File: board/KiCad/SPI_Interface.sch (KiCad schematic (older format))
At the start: 6 parts

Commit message: Finalize first draft
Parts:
- J2: renamed from J?; footprint Pinhead_1x6_TH -> Pin_Headers:Pin_Header_Straight_1x06
- R10, R11, R6, R9: renamed from R?; footprint (none) -> Resistors_SMD:R_0603_HandSoldering
- U4: renamed from U?; footprint (none) -> pmod:SOP2-8_Handsoldering
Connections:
- net 3V3_PMOD: now also U4.8 (VDD)
- net EXT_SPI_CLK: now also J2.2; no longer J2.4
- net EXT_SPI_MISO: now also J2.4; no longer J2.2
- no-connect marks 1 -> 0
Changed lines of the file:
@@
 $EndDescr
 $Comp
-L N25Q U?
+L N25Q U4
 U 1 1 56BBB08B
 P 5250 2850
-F 0 "U?" H 5050 2300 60  0000 C CNN
+F 0 "U4" H 5050 2300 60  0000 C CNN
 F 1 "N25Q" H 4950 3750 60  0000 C CNN
-F 2 "" H 5250 2850 60  0000 C CNN
+F 2 "pmod:SOP2-8_Handsoldering" H 5250 2850 60  0001 C CNN
 F 3 "" H 5250 2850 60  0000 C CNN
 	1    5250 2850
@@
 Wire Wire Line
 	1600 1300 7550 1300
-Wire Wire Line
-	5250 1300 5250 1900
-$Comp
-L GND #PWR?
+$Comp
+L GND #PWR22
 U 1 1 56BCE787
 P 5250 3800
-F 0 "#PWR?" H 5250 3550 50  0001 C CNN
+F 0 "#PWR22" H 5250 3550 50  0001 C CNN
 F 1 "GND" H 5250 3650 50  0000 C CNN
 F 2 "" H 5250 3800 60  0000 C CNN
@@
 	5250 3800 5250 3500
 $Comp
-L R R?
+L R R9
 U 1 1 56BCEBB1
 P 7050 2500
-F 0 "R?" V 7130 2500 50  0000 C CNN
+F 0 "R9" V 7130 2500 50  0000 C CNN
 F 1 "10k" V 7050 2500 50  0000 C CNN
-F 2 "" V 6980 2500 30  0000 C CNN
+F 2 "Resistors_SMD:R_0603_HandSoldering" V 6980 2500 30  0001 C CNN
 F 3 "" H 7050 2500 30  0000 C CNN
 	1    7050 2500
@@
 $EndComp
 $Comp
-L R R?
+L R R10
 U 1 1 56BCEC4A
 P 7300 2500
-F 0 "R?" V 7380 2500 50  0000 C CNN
+F 0 "R10" V 7380 2500 50  0000 C CNN
 F 1 "10k" V 7300 2500 50  0000 C CNN
-F 2 "" V 7230 2500 30  0000 C CNN
+F 2 "Resistors_SMD:R_0603_HandSoldering" V 7230 2500 30  0001 C CNN
 F 3 "" H 7300 2500 30  0000 C CNN
 	1    7300 2500
@@
 $EndComp
 $Comp
-L R R?
+L R R11
 U 1 1 56BCEC79
 P 7550 2500
-F 0 "R?" V 7630 2500 50  0000 C CNN
+F 0 "R11" V 7630 2500 50  0000 C CNN
 F 1 "10k" V 7550 2500 50  0000 C CNN
-F 2 "" V 7480 2500 30  0000 C CNN
+F 2 "Resistors_SMD:R_0603_HandSoldering" V 7480 2500 30  0001 C CNN
 F 3 "" H 7550 2500 30  0000 C CNN
 	1    7550 2500
@@
 EXT_SPI_SS_B
 Connection ~ 4400 2950
-NoConn ~ 8200 1800
 Text GLabel 1550 2150 0    60   Input ~ 0
 ICE_SDO
@@
 ICE_SDI
 Wire Wire Line
-	5900 2350 5950 2350
-Wire Wire Line
-	5950 2350 5950 1950
-Wire Wire Line
-	5950 1950 1550 1950
+	5950 2350 5900 2350
+Wire Wire Line
+	5950 1800 5950 2350
 Text GLabel 1700 2800 0    60   Input ~ 0
 EXT_SPI_MISO
@@
 Connection ~ 3650 2350
 $Comp
-L R R?
+L R R6
 U 1 1 56BD0F26
 P 4350 1600
-F 0 "R?" V 4430 1600 50  0000 C CNN
+F 0 "R6" V 4430 1600 50  0000 C CNN
 F 1 "10k" V 4350 1600 50  0000 C CNN
-F 2 "" V 4280 1600 30  0000 C CNN
+F 2 "Resistors_SMD:R_0603_HandSoldering" V 4280 1600 30  0001 C CNN
 F 3 "" H 4350 1600 30  0000 C CNN
 	1    4350 1600
@@
 Connection ~ 3450 2450
 $Comp
-L Pinheader_1x6_TH J?
+L Pinheader_1x6_TH J2
 U 1 1 56BD1B95
 P 1500 6000
-F 0 "J?" H 1500 6340 60  0000 C CNN
+F 0 "J2" H 1500 6340 60  0000 C CNN
 F 1 "Pinheader_1x6_TH" H 1540 6580 60  0001 C CNN
-F 2 "Pinhead_1x6_TH" H 1540 6470 60  0001 C CNN
+F 2 "Pin_Headers:Pin_Header_Straight_1x06" H 1540 6470 60  0001 C CNN
 F 3 "" H 1500 6000 60  0000 C CNN
 F 4 "609-3263-ND" H 1560 7120 60  0001 C CNN "Vendor Part Number"
@@
 Text GLabel 1750 5950 2    60   Input ~ 0
 EXT_SPI_MOSI
-Text GLabel 1750 5850 2    60   Input ~ 0
+Text GLabel 1750 6050 2    60   Input ~ 0
 EXT_SPI_MISO
 Text GLabel 1750 5750 2    60   Input ~ 0
 3V3_PMOD
-Text GLabel 1750 6050 2    60   Input ~ 0
+Text GLabel 1750 5850 2    60   Input ~ 0
 EXT_SPI_CLK
 Text GLabel 1750 6150 2    60   Input ~ 0
 EXT_SPI_SS_B
 $Comp
-L GND #PWR?
+L GND #PWR2
 U 1 1 56BD1F49
 P 2000 6400
-F 0 "#PWR?" H 2000 6150 50  0001 C CNN
+F 0 "#PWR2" H 2000 6150 50  0001 C CNN
 F 1 "GND" H 2000 6250 50  0000 C CNN
 F 2 "" H 2000 6400 60  0000 C CNN
@@
 Text Notes 750  2450 0    60   ~ 0
 to iCE
+Wire Wire Line
+	5250 1850 5250 1300
+Wire Wire Line
+	1550 1950 4600 1950
+Wire Wire Line
+	4600 1950 4600 1800
+Wire Wire Line
+	4600 1800 5950 1800
 $EndSCHEMATC

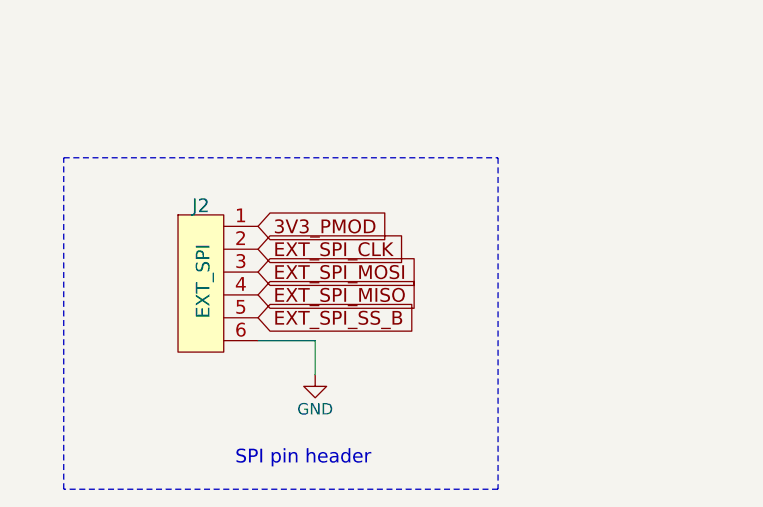
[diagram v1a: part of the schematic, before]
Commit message: Improve design
* PMOS on input voltage for polarity
* Re-design board to add mount holes and better routing
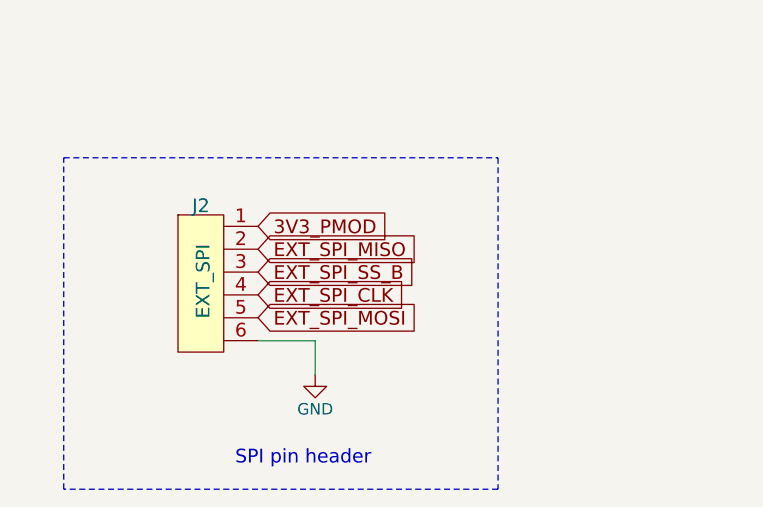
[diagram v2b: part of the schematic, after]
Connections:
- net EXT_SPI_CLK: now also J2.4; no longer J2.2
- net EXT_SPI_MISO: now also J2.2; no longer J2.4
- net EXT_SPI_MOSI: now also J2.5; no longer J2.3
- net EXT_SPI_SS_B: now also J2.3; no longer J2.5
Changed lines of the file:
@@
 	1600 1300 7550 1300
 $Comp
-L GND #PWR22
+L GND #PWR37
 U 1 1 56BCE787
 P 5250 3800
-F 0 "#PWR22" H 5250 3550 50  0001 C CNN
+F 0 "#PWR37" H 5250 3550 50  0001 C CNN
 F 1 "GND" H 5250 3650 50  0000 C CNN
 F 2 "" H 5250 3800 60  0000 C CNN
@@
 	1    0    0    -1
 $EndComp
-Text GLabel 1750 5950 2    60   Input ~ 0
+Text GLabel 1750 6150 2    60   Input ~ 0
 EXT_SPI_MOSI
-Text GLabel 1750 6050 2    60   Input ~ 0
+Text GLabel 1750 5850 2    60   Input ~ 0
 EXT_SPI_MISO
 Text GLabel 1750 5750 2    60   Input ~ 0
 3V3_PMOD
-Text GLabel 1750 5850 2    60   Input ~ 0
+Text GLabel 1750 6050 2    60   Input ~ 0
 EXT_SPI_CLK
-Text GLabel 1750 6150 2    60   Input ~ 0
+Text GLabel 1750 5950 2    60   Input ~ 0
 EXT_SPI_SS_B
 $Comp
-L GND #PWR2
+L GND #PWR36
 U 1 1 56BD1F49
 P 2000 6400
-F 0 "#PWR2" H 2000 6150 50  0001 C CNN
+F 0 "#PWR36" H 2000 6150 50  0001 C CNN
 F 1 "GND" H 2000 6250 50  0000 C CNN
 F 2 "" H 2000 6400 60  0000 C CNN

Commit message: Housekeeping
Structure libraries and put proper licenses to them.
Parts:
- U4: footprint pmod:SOP2-8_Handsoldering -> lms6002-pmod:SOP2-8_Handsoldering
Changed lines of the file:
@@
 LIBS:contrib
 LIBS:valves
+LIBS:lms6002-pmod
 LIBS:ice40_1k4k_tq144
 LIBS:myriad
-LIBS:pmod
-LIBS:LMS6002-Pmod-cache
 EELAYER 25 0
 EELAYER END
@@
 F 0 "U4" H 5050 2300 60  0000 C CNN
 F 1 "N25Q" H 4950 3750 60  0000 C CNN
-F 2 "pmod:SOP2-8_Handsoldering" H 5250 2850 60  0001 C CNN
+F 2 "lms6002-pmod:SOP2-8_Handsoldering" H 5250 2850 60  0001 C CNN
 F 3 "" H 5250 2850 60  0000 C CNN
 	1    5250 2850
